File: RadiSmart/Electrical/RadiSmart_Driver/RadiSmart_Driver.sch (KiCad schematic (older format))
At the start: 18 parts, among them P2 CONN_01X07, P3 CONN_01X07

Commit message: added more datasheets for interesting chips, temperature sensing and real-time clock
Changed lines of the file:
@@
 LIBS:contrib
 LIBS:valves
-LIBS:MRV_ICs
 LIBS:RadiSmart_Driver-cache
 EELAYER 25 0
@@
 F2 "PWM3" I R 6400 3800 60
 F3 "ADC1" I R 6400 3100 60
-F4 "ADC2" I R 6400 3200 60
-F5 "ADC3" I R 6400 3900 60
+F4 "ADC2" I R 6400 4450 60
+F5 "ADC3" I R 6400 4550 60
 F6 "ADC4" I R 6400 4000 60
-F7 "ADC5" I L 5150 4150 60
-F8 "ADC6" I L 5150 4050 60
+F7 "ADC5" I R 6400 3900 60
+F8 "ADC6" I R 6400 3200 60
 F9 "PWM2" I R 6400 3700 60
 F10 "PWM1" I R 6400 3000 60

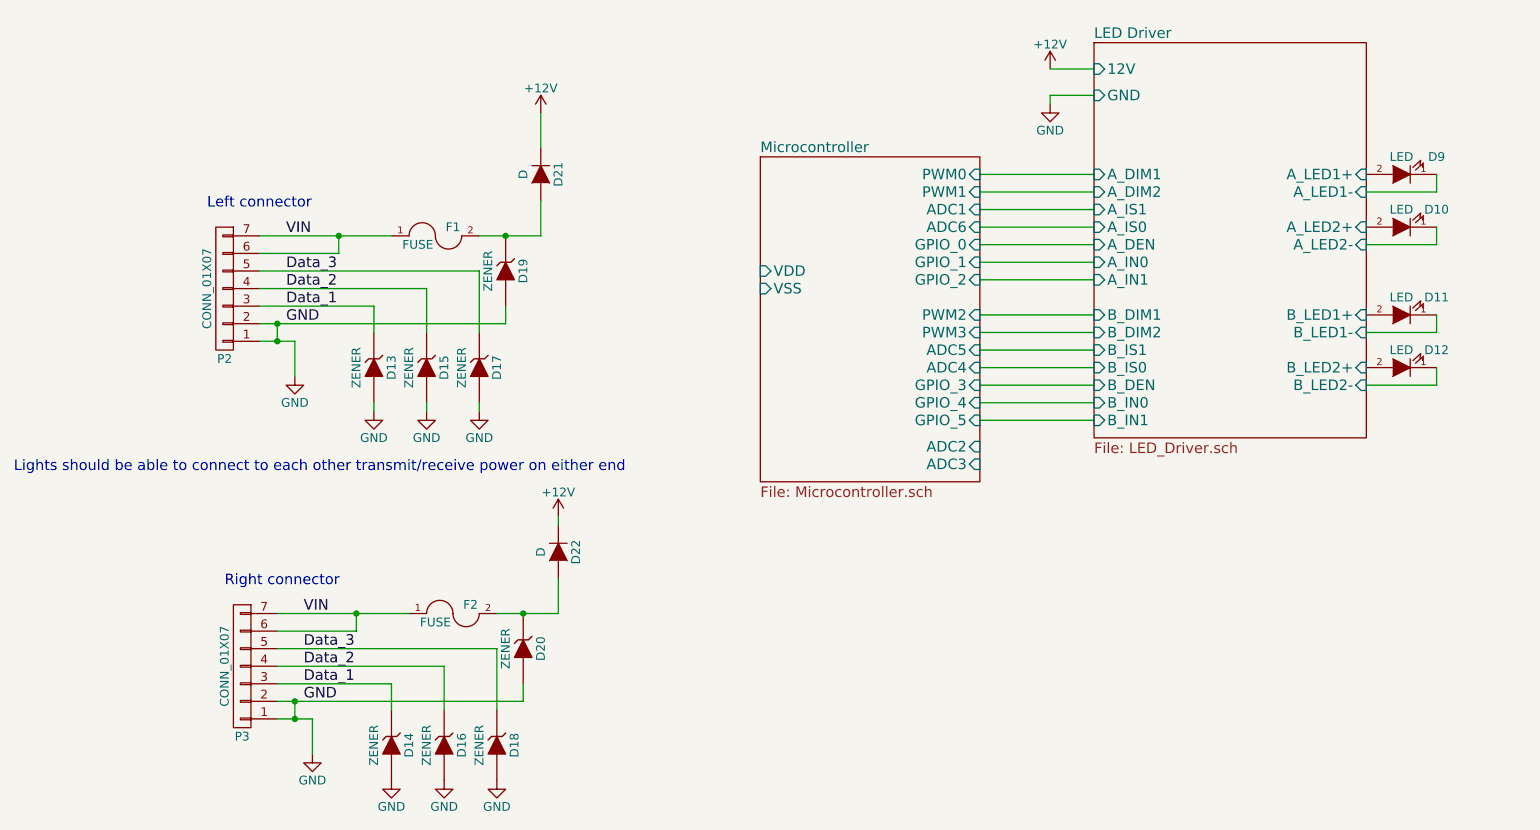
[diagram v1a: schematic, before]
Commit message: switching from 12V to 24V to support more LEDs per channel
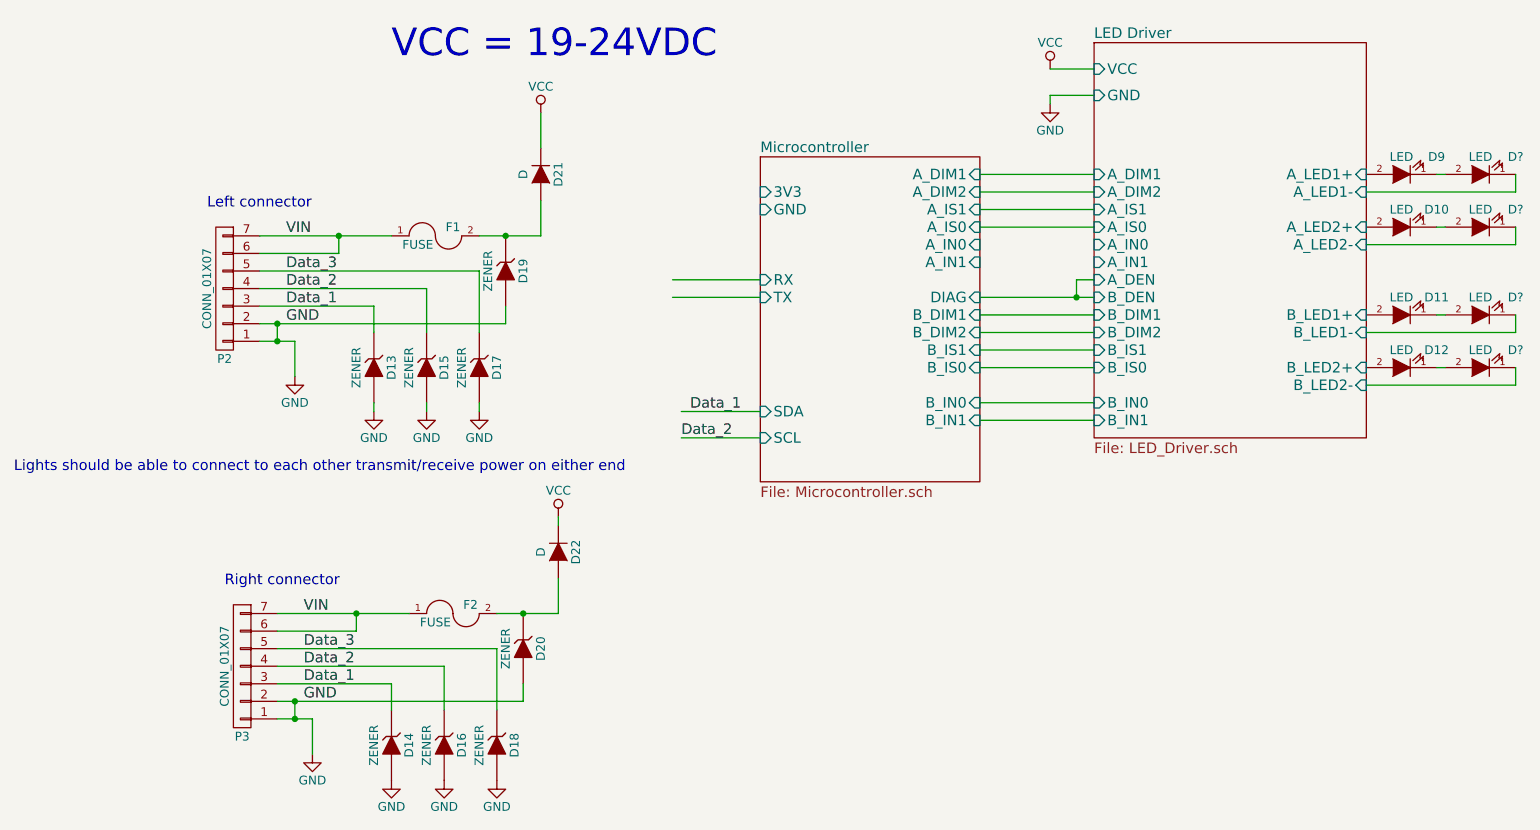
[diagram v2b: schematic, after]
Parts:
- added D? (x4): LED, MRV_SMD_Packages:CREE_LED_2020, symbol LED
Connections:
- net labels added: VCC
- net labels removed: +12V
- wire segments 62 -> 69
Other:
- note added: "VCC = 19-24VDC\n"
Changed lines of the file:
@@
 LIBS:contrib
 LIBS:valves
+LIBS:MRV_ICs
 LIBS:RadiSmart_Driver-cache
 EELAYER 25 0
@@
 F0 "LED Driver" 60
 F1 "LED_Driver.sch" 60
-F2 "12V" I L 7050 2300 60
-F3 "GND" I L 7050 2450 60
-F4 "A_DIM1" I L 7050 2900 60
-F5 "A_LED1+" I R 8600 2900 60
-F6 "A_LED1-" I R 8600 3000 60
-F7 "A_DIM2" I L 7050 3000 60
-F8 "A_LED2+" I R 8600 3200 60
-F9 "A_LED2-" I R 8600 3300 60
-F10 "A_IS1" I L 7050 3100 60
-F11 "A_IS0" I L 7050 3200 60
-F12 "A_DEN" I L 7050 3300 60
-F13 "A_IN0" I L 7050 3400 60
-F14 "A_IN1" I L 7050 3500 60
-F15 "B_DIM1" I L 7050 3700 60
-F16 "B_LED1+" I R 8600 3700 60
-F17 "B_LED1-" I R 8600 3800 60
-F18 "B_DIM2" I L 7050 3800 60
-F19 "B_LED2+" I R 8600 4000 60
-F20 "B_LED2-" I R 8600 4100 60
-F21 "B_IS1" I L 7050 3900 60
-F22 "B_IS0" I L 7050 4000 60
-F23 "B_DEN" I L 7050 4100 60
-F24 "B_IN0" I L 7050 4200 60
-F25 "B_IN1" I L 7050 4300 60
-$EndSheet
-$Sheet
-S 5150 2800 1250 1850
-U 59F58DA5
-F0 "Microcontroller" 60
-F1 "Microcontroller.sch" 60
-F2 "PWM3" I R 6400 3800 60
-F3 "ADC1" I R 6400 3100 60
-F4 "ADC2" I R 6400 4450 60
-F5 "ADC3" I R 6400 4550 60
-F6 "ADC4" I R 6400 4000 60
-F7 "ADC5" I R 6400 3900 60
-F8 "ADC6" I R 6400 3200 60
-F9 "PWM2" I R 6400 3700 60
-F10 "PWM1" I R 6400 3000 60
-F11 "PWM0" I R 6400 2900 60
-F12 "GPIO_0" I R 6400 3300 60
-F13 "GPIO_1" I R 6400 3400 60
-F14 "GPIO_2" I R 6400 3500 60
-F15 "GPIO_3" I R 6400 4100 60
-F16 "GPIO_4" I R 6400 4200 60
-F17 "GPIO_5" I R 6400 4300 60
-F18 "VDD" I L 5150 3450 60
-F19 "VSS" I L 5150 3550 60
+F2 "GND" I L 7050 2450 60
+F3 "A_DIM1" I L 7050 2900 60
+F4 "A_LED1+" I R 8600 2900 60
+F5 "A_LED1-" I R 8600 3000 60
+F6 "A_DIM2" I L 7050 3000 60
+F7 "A_LED2+" I R 8600 3200 60
+F8 "A_LED2-" I R 8600 3300 60
+F9 "A_IS1" I L 7050 3100 60
+F10 "A_IS0" I L 7050 3200 60
+F11 "A_DEN" I L 7050 3500 60
+F12 "A_IN0" I L 7050 3300 60
+F13 "A_IN1" I L 7050 3400 60
+F14 "B_DIM1" I L 7050 3700 60
+F15 "B_LED1+" I R 8600 3700 60
+F16 "B_LED1-" I R 8600 3800 60
+F17 "B_DIM2" I L 7050 3800 60
+F18 "B_LED2+" I R 8600 4000 60
+F19 "B_LED2-" I R 8600 4100 60
+F20 "B_IS1" I L 7050 3900 60
+F21 "B_IS0" I L 7050 4000 60
+F22 "B_DEN" I L 7050 3600 60
+F23 "B_IN0" I L 7050 4200 60
+F24 "B_IN1" I L 7050 4300 60
+F25 "VCC" I L 7050 2300 60
 $EndSheet
 $Comp
@@
 F 3 "" H 2500 4050 50  0000 C CNN
 	1    2500 4050
-	1    0    0    -1
-$EndComp
-$Comp
-L +12V #PWR02
-U 1 1 59F6A4D6
-P 3900 2550
-F 0 "#PWR02" H 3900 2400 50  0001 C CNN
-F 1 "+12V" H 3900 2690 50  0000 C CNN
-F 2 "" H 3900 2550 50  0000 C CNN
-F 3 "" H 3900 2550 50  0000 C CNN
-	1    3900 2550
 	1    0    0    -1
 $EndComp
@@
 $EndComp
 $Comp
-L +12V #PWR07
-U 1 1 59F74399
-P 4000 4850
-F 0 "#PWR07" H 4000 4700 50  0001 C CNN
-F 1 "+12V" H 4000 4990 50  0000 C CNN
-F 2 "" H 4000 4850 50  0000 C CNN
-F 3 "" H 4000 4850 50  0000 C CNN
-	1    4000 4850
-	1    0    0    -1
-$EndComp
-$Comp
 L ZENER D20
 U 1 1 59F7439F
@@
 Lights should be able to connect to each other transmit/receive power on either end
 $Comp
-L +12V #PWR011
-U 1 1 59F7608A
-P 6800 2300
-F 0 "#PWR011" H 6800 2150 50  0001 C CNN
-F 1 "+12V" H 6800 2440 50  0000 C CNN
-F 2 "" H 6800 2300 50  0000 C CNN
-F 3 "" H 6800 2300 50  0000 C CNN
-	1    6800 2300
-	1    0    0    -1
-$EndComp
-$Comp
 L GND #PWR012
 U 1 1 59F76658
@@
 	1    0    0    -1
 $EndComp
+$Comp
+L LED D?
+U 1 1 5A05A343
+P 9250 2900
+F 0 "D?" H 9050 2800 50  0000 C CNN
+F 1 "LED" H 9250 2800 50  0000 C CNN
+F 2 "MRV_SMD_Packages:CREE_LED_2020" H 9250 2900 50  0001 C CNN
+F 3 "" H 9250 2900 50  0000 C CNN
+	1    9250 2900
+	-1   0    0    1
+$EndComp
+$Comp
+L LED D?
+U 1 1 5A05AAC9
+P 9250 3200
+F 0 "D?" H 9050 3100 50  0000 C CNN
+F 1 "LED" H 9250 3100 50  0000 C CNN
+F 2 "MRV_SMD_Packages:CREE_LED_2020" H 9250 3200 50  0001 C CNN
+F 3 "" H 9250 3200 50  0000 C CNN
+	1    9250 3200
+	-1   0    0    1
+$EndComp
+$Comp
+L LED D?
+U 1 1 5A05B0B0
+P 9250 3700
+F 0 "D?" H 9050 3600 50  0000 C CNN
+F 1 "LED" H 9250 3600 50  0000 C CNN
+F 2 "MRV_SMD_Packages:CREE_LED_2020" H 9250 3700 50  0001 C CNN
+F 3 "" H 9250 3700 50  0000 C CNN
+	1    9250 3700
+	-1   0    0    1
+$EndComp
+$Comp
+L LED D?
+U 1 1 5A05B4EC
+P 9250 4000
+F 0 "D?" H 9050 3900 50  0000 C CNN
+F 1 "LED" H 9250 3900 50  0000 C CNN
+F 2 "MRV_SMD_Packages:CREE_LED_2020" H 9250 4000 50  0001 C CNN
+F 3 "" H 9250 4000 50  0000 C CNN
+	1    9250 4000
+	-1   0    0    1
+$EndComp
+$Comp
+L VCC #PWR?
+U 1 1 5A05D6C2
+P 3900 2550
+F 0 "#PWR?" H 3900 2400 50  0001 C CNN
+F 1 "VCC" H 3900 2700 50  0000 C CNN
+F 2 "" H 3900 2550 50  0000 C CNN
+F 3 "" H 3900 2550 50  0000 C CNN
+	1    3900 2550
+	1    0    0    -1
+$EndComp
+$Comp
+L VCC #PWR?
+U 1 1 5A05E6AF
+P 6800 2300
+F 0 "#PWR?" H 6800 2150 50  0001 C CNN
+F 1 "VCC" H 6800 2450 50  0000 C CNN
+F 2 "" H 6800 2300 50  0000 C CNN
+F 3 "" H 6800 2300 50  0000 C CNN
+	1    6800 2300
+	1    0    0    -1
+$EndComp
+$Comp
+L VCC #PWR?
+U 1 1 5A05F084
+P 4000 4850
+F 0 "#PWR?" H 4000 4700 50  0001 C CNN
+F 1 "VCC" H 4000 5000 50  0000 C CNN
+F 2 "" H 4000 4850 50  0000 C CNN
+F 3 "" H 4000 4850 50  0000 C CNN
+	1    4000 4850
+	1    0    0    -1
+$EndComp
+Text Notes 3050 2250 0    157  ~ 0
+VCC = 19-24VDC\n
+$Sheet
+S 5150 2800 1250 1850
+U 59F58DA5
+F0 "Microcontroller" 60
+F1 "Microcontroller.sch" 60
+F2 "A_DIM1" I R 6400 2900 60
+F3 "3V3" I L 5150 3000 60
+F4 "GND" I L 5150 3100 60
+F5 "B_DIM2" I R 6400 3800 60
+F6 "B_DIM1" I R 6400 3700 60
+F7 "A_DIM2" I R 6400 3000 60
+F8 "A_IN0" I R 6400 3300 60
+F9 "A_IN1" I R 6400 3400 60
+F10 "B_IN0" I R 6400 4200 60
+F11 "B_IN1" I R 6400 4300 60
+F12 "B_IS0" I R 6400 4000 60
+F13 "A_IS0" I R 6400 3200 60
+F14 "A_IS1" I R 6400 3100 60
+F15 "B_IS1" I R 6400 3900 60
+F16 "RX" I L 5150 3500 60
+F17 "TX" I L 5150 3600 60
+F18 "DIAG" I R 6400 3600 60
+F19 "SCL" I L 5150 4400 60
+F20 "SDA" I L 5150 4250 60
+$EndSheet
 Wire Wire Line
 	6400 2900 7050 2900
@@
 	6400 3200 7050 3200
 Wire Wire Line
-	6400 3300 7050 3300
-Wire Wire Line
-	6400 3400 7050 3400
-Wire Wire Line
-	7050 3500 6400 3500
-Wire Wire Line
 	6400 3700 7050 3700
 Wire Wire Line
@@
 	7050 4000 6400 4000
 Wire Wire Line
-	6400 4100 7050 4100
-Wire Wire Line
 	7050 4200 6400 4200
 Wire Wire Line
 	6400 4300 7050 4300
 Wire Wire Line
-	8600 4100 9000 4100
-Wire Wire Line
-	9000 4100 9000 4000
-Wire Wire Line
-	8600 3800 9000 3800
-Wire Wire Line
-	8600 3300 9000 3300
-Wire Wire Line
-	9000 3300 9000 3200
-Wire Wire Line
-	8600 3000 9000 3000
-Wire Wire Line
-	9000 3000 9000 2900
-Wire Wire Line
-	9000 3800 9000 3700
+	8600 4100 9450 4100
+Wire Wire Line
+	8600 3800 9450 3800
+Wire Wire Line
+	8600 3000 9450 3000
 Wire Wire Line
 	2300 3850 2500 3850
@@
 Wire Wire Line
 	4000 4900 4000 4850
+Wire Wire Line
+	9000 2900 9050 2900
+Wire Wire Line
+	9450 3000 9450 2900
+Wire Wire Line
+	9000 3700 9050 3700
+Wire Wire Line
+	9450 3800 9450 3700
+Wire Wire Line
+	9000 4000 9050 4000
+Wire Wire Line
+	9450 4100 9450 4000
+Wire Wire Line
+	9000 3200 9050 3200
+Wire Wire Line
+	8600 3300 9450 3300
+Wire Wire Line
+	9450 3300 9450 3200
+Wire Wire Line
+	6400 3600 7050 3600
+Wire Wire Line
+	6950 3600 6950 3500
+Wire Wire Line
+	6950 3500 7050 3500
+Connection ~ 6950 3600
+Text Label 4750 4250 0    60   ~ 0
+Data_1
+Text Label 4700 4400 0    60   ~ 0
+Data_2
+Wire Wire Line
+	5150 3600 4650 3600
+Wire Wire Line
+	5150 3500 4650 3500
+Wire Wire Line
+	4700 4250 5150 4250
+Wire Wire Line
+	5150 4400 4700 4400
 $EndSCHEMATC
